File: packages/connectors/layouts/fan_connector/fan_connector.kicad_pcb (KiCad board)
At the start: 2 copper layers, 1 part

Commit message: WIP update packages till ESPs
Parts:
- CN1: footprint lib:CONN-TH_4P-P2.54_HCTL_HC-2510-4A -> HCTL_HC_2510_4A:CONN-TH_4P-P2.54_HCTL_HC-2510-4A
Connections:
- CN1 pad 1: line-1 -> line
- CN1 pad 2: line -> line-1

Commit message: Manually fix fp lib tables
fix some small bugs
fix package only modules (e.g. logos)
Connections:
- CN1 pad 1: line -> line-1
- CN1 pad 2: line-1 -> line
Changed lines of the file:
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@@
     (net 0 "")
     (net 1 "hv")
-    (net 2 "line")
-    (net 3 "line-1")
+    (net 2 "line-1")
+    (net 3 "line")
     (net 4 "gnd")
     (footprint "HCTL_HC_2510_4A:CONN-TH_4P-P2.54_HCTL_HC-2510-4A"
@@
             (drill 1.100023)
             (layers "*.Cu" "*.Mask")
-            (net 2 "line")
+            (net 2 "line-1")
             (remove_unused_layers no)
         )
@@
             (drill 1.100023)
             (layers "*.Cu" "*.Mask")
-            (net 3 "line-1")
+            (net 3 "line")
             (remove_unused_layers no)
         )

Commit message: rebuild all packages & regenerate images of changed layouts (silk)
Add new scripts for version bump and build (based on atopile/packages)
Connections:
- CN1 pad 1: line-1 -> line
- CN1 pad 2: line -> line-1

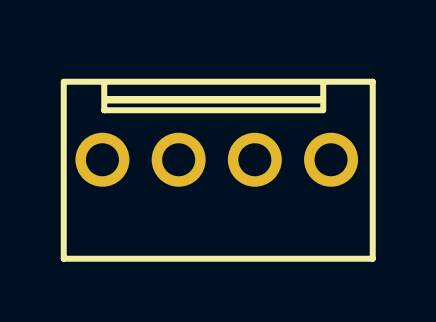
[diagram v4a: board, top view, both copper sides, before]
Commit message: Fix fan connector
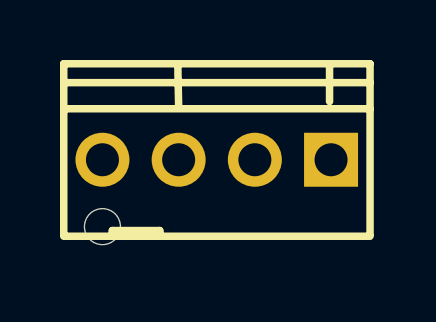
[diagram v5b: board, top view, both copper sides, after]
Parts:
- CN1: footprint HCTL_HC_2510_4A:CONN-TH_4P-P2.54_HCTL_HC-2510-4A -> PINREX_744_81_04TG20:CONN-TH_4P-P2.54-V-M_744-81-04TXXX
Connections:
- CN1 pad 1: line -> gnd
- CN1 pad 2: line-1 -> hv
- CN1 pad 3: hv -> line
- CN1 pad 4: gnd -> line-1
